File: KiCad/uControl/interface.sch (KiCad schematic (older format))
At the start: 66 parts, among them M1 MANIFOLD, P10 C3SB, P11 VSel_Vlv, P12 Valve_Conn, P13 Valve_Conn_BO, P14 Valve, P15 Flow_Conn, P16 FlowMeter, P17 Pump_Conn, P18 Pump_Conn_BO, P19 Pump_Conn_Flex, P20 Temp_Conn, P21 Temp_Conn_BO, P22 Temp, P23 Pump, P6 Pulse, P7 Gage_Pr, P8 Abso_Pr, P9 C3SB, Q1 2SD1834T100, U1 TXB0104D, U2 TXS0102DCT

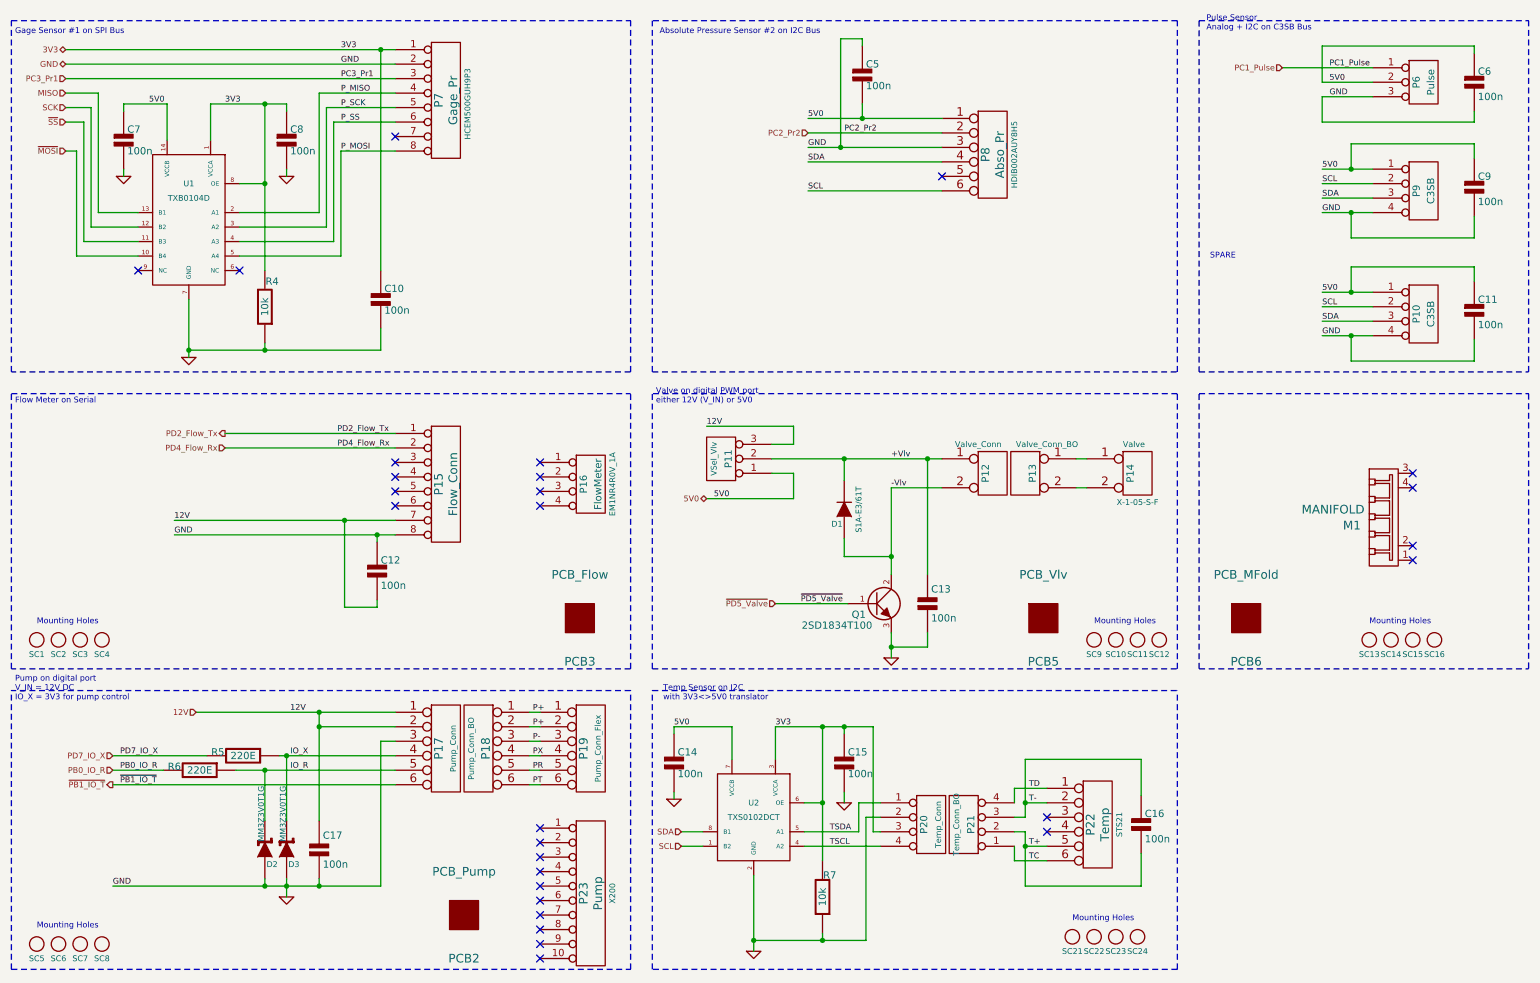
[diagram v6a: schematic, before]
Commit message: uControl track layout complete. Needs to be checked.
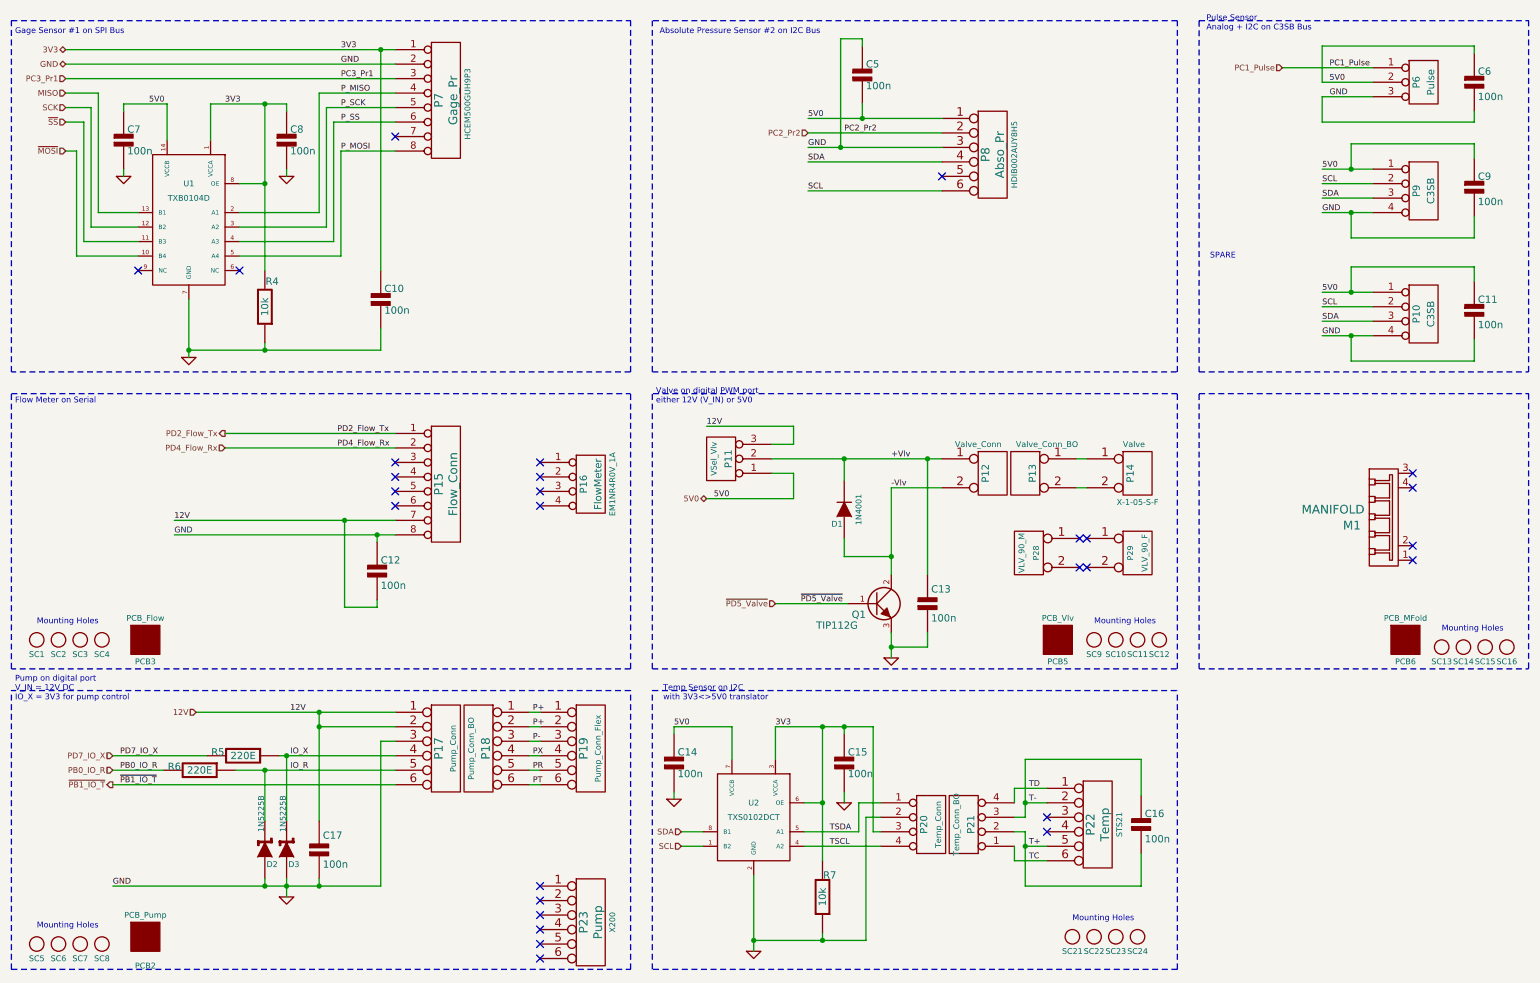
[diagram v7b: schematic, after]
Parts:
- removed P23: Pump, Pump, symbol CONN_10
- added P23: Pump, symbol CONN_6
- added P28: VLV_90_M, 2X06/90, symbol CONN_2
- added P29: VLV_90_F, Header_F_6x2, symbol CONN_2
- D1: value S1A-E3/61T -> 1N4001
- D2, D3: value MM3Z3V0T1G -> 1N5225B
- Q1: value 2SD1834T100 -> TIP112G
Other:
- moved on the sheet: PCB2, PCB3, PCB5, PCB6, SC13, SC14, SC15, SC16
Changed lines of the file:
@@
-EESchema Schematic File Version 2  date Friday 28 December 2012 10:02:48 PM IST
+EESchema Schematic File Version 2  date 12/29/2012 7:23:44 PM
 LIBS:uControl
 LIBS:Conn-raspberry
@@
 Sheet 2 5
 Title ""
-Date "28 dec 2012"
+Date "29 dec 2012"
 Rev ""
 Comp ""
@@
 Comment4 ""
 $EndDescr
+$Comp
+L CONN_6 P23
+U 1 1 50DED8EA
+P 4675 6800
+F 0 "P23" V 4625 6800 60  0000 C CNN
+F 1 "Pump" V 4725 6800 60  0000 C CNN
+F 4 "X200" V 4825 6800 40  0000 C CNN "Part_No"
+	1    4675 6800
+	1    0    0    -1
+$EndComp
+NoConn ~ 8050 4350
+NoConn ~ 8100 4350
+NoConn ~ 8100 4150
+NoConn ~ 8050 4150
+$Comp
+L CONN_2 P28
+U 1 1 50DE8768
+P 7700 4250
+F 0 "P28" V 7650 4250 40  0000 C CNN
+F 1 "VLV_90_M" V 7750 4250 40  0000 C CNN
+F 2 "2X06/90" V 7850 4250 40  0001 C CNN
+	1    7700 4250
+	-1   0    0    -1
+$EndComp
+$Comp
+L CONN_2 P29
+U 1 1 50DE8761
+P 8450 4250
+F 0 "P29" V 8400 4250 40  0000 C CNN
+F 1 "VLV_90_F" V 8500 4250 40  0000 C CNN
+F 2 "Header_F_6x2" V 8600 4250 40  0001 C CNN
+	1    8450 4250
+	1    0    0    -1
+$EndComp
 Text Label 6750 3600 0    40   ~ 0
 +Vlv
@@
 L PCB PCB6
 U 1 1 50DAE3BE
-P 9200 4700
-F 0 "PCB6" H 9200 4400 60  0000 C CNN
-F 1 "PCB_MFold" H 9200 5000 60  0000 C CNN
-F 2 "PCB_Mfold" H 9200 5100 60  0001 C CNN
-	1    9200 4700
+P 10300 4850
+F 0 "PCB6" H 10300 4700 40  0000 C CNN
+F 1 "PCB_MFold" H 10300 5000 40  0000 C CNN
+F 2 "PCB_Mfold" H 10300 5250 40  0001 C CNN
+	1    10300 4850
 	1    0    0    -1
 $EndComp
@@
 L PCB PCB5
 U 1 1 50DAE3A7
-P 7800 4700
-F 0 "PCB5" H 7800 4400 60  0000 C CNN
-F 1 "PCB_Vlv" H 7800 5000 60  0000 C CNN
-F 2 "PCB_Vlv" H 7800 5100 60  0001 C CNN
-	1    7800 4700
+P 7900 4850
+F 0 "PCB5" H 7900 4700 40  0000 C CNN
+F 1 "PCB_Vlv" H 7900 5000 40  0000 C CNN
+F 2 "PCB_Vlv" H 7900 5250 40  0001 C CNN
+	1    7900 4850
 	1    0    0    -1
 $EndComp
@@
 L PCB PCB2
 U 1 1 50DAE394
-P 3800 6750
-F 0 "PCB2" H 3800 6450 60  0000 C CNN
-F 1 "PCB_Pump" H 3800 7050 60  0000 C CNN
-F 2 "PCB_Pump" H 3800 7150 60  0001 C CNN
-	1    3800 6750
+P 1600 6900
+F 0 "PCB2" H 1600 6700 40  0000 C CNN
+F 1 "PCB_Pump" H 1600 7050 40  0000 C CNN
+F 2 "PCB_Pump" H 1600 7300 40  0001 C CNN
+	1    1600 6900
 	1    0    0    -1
 $EndComp
@@
 L PCB PCB3
 U 1 1 50DAE38C
-P 4600 4700
-F 0 "PCB3" H 4600 4400 60  0000 C CNN
-F 1 "PCB_Flow" H 4600 5000 60  0000 C CNN
-F 2 "PCB_Flow" H 4600 5100 60  0001 C CNN
-	1    4600 4700
+P 1600 4850
+F 0 "PCB3" H 1600 4700 40  0000 C CNN
+F 1 "PCB_Flow" H 1600 5000 40  0000 C CNN
+F 2 "PCB_Flow" H 1600 5250 40  0001 C CNN
+	1    1600 4850
 	1    0    0    -1
 $EndComp
@@
 Wire Notes Line
 	11150 3150 11150 5050
-Text Notes 10050 4750 0    40   ~ 0
+Text Notes 10550 4800 0    40   ~ 0
 Mounting Holes
 $Comp
 L SCREW SC16
 U 1 1 50DAD9E8
-P 10500 4850
-F 0 "SC16" H 10500 4750 40  0000 C CNN
-F 1 "SCREW" H 10500 4950 40  0001 C CNN
-F 2 "vite_3mm" H 10500 5050 40  0001 C CNN
-	1    10500 4850
+P 11000 4900
+F 0 "SC16" H 11000 4800 40  0000 C CNN
+F 1 "SCREW" H 11000 5000 40  0001 C CNN
+F 2 "vite_3mm" H 11000 5100 40  0001 C CNN
+	1    11000 4900
 	1    0    0    -1
 $EndComp
@@
 L SCREW SC15
 U 1 1 50DAD9E7
-P 10350 4850
-F 0 "SC15" H 10350 4750 40  0000 C CNN
-F 1 "SCREW" H 10350 4950 40  0001 C CNN
-F 2 "vite_3mm" H 10350 5050 40  0001 C CNN
-	1    10350 4850
+P 10850 4900
+F 0 "SC15" H 10850 4800 40  0000 C CNN
+F 1 "SCREW" H 10850 5000 40  0001 C CNN
+F 2 "vite_3mm" H 10850 5100 40  0001 C CNN
+	1    10850 4900
 	1    0    0    -1
 $EndComp
@@
 L SCREW SC14
 U 1 1 50DAD9E6
-P 10200 4850
-F 0 "SC14" H 10200 4750 40  0000 C CNN
-F 1 "SCREW" H 10200 4950 40  0001 C CNN
-F 2 "vite_3mm" H 10200 5050 40  0001 C CNN
-	1    10200 4850
+P 10700 4900
+F 0 "SC14" H 10700 4800 40  0000 C CNN
+F 1 "SCREW" H 10700 5000 40  0001 C CNN
+F 2 "vite_3mm" H 10700 5100 40  0001 C CNN
+	1    10700 4900
 	1    0    0    -1
 $EndComp
@@
 L SCREW SC13
 U 1 1 50DAD9E5
-P 10050 4850
-F 0 "SC13" H 10050 4750 40  0000 C CNN
-F 1 "SCREW" H 10050 4950 40  0001 C CNN
-F 2 "vite_3mm" H 10050 5050 40  0001 C CNN
-	1    10050 4850
+P 10550 4900
+F 0 "SC13" H 10550 4800 40  0000 C CNN
+F 1 "SCREW" H 10550 5000 40  0001 C CNN
+F 2 "vite_3mm" H 10550 5100 40  0001 C CNN
+	1    10550 4900
 	1    0    0    -1
 $EndComp
@@
 NoConn ~ 4325 6750
 $Comp
-L CONN_10 P23
-U 1 1 50D6C18B
-P 4675 6600
-F 0 "P23" V 4625 6600 60  0000 C CNN
-F 1 "Pump" V 4725 6600 60  0000 C CNN
-F 2 "Pump" V 4825 6600 60  0001 C CNN
-F 4 "X200" V 4825 6600 40  0000 C CNN "Part_No"
-	1    4675 6600
-	1    0    0    -1
-$EndComp
-$Comp
 L CONN_4 P16
 U 1 1 50D6BF9C
@@
 NoConn ~ 4325 6650
 NoConn ~ 4325 6550
-NoConn ~ 4325 6450
-NoConn ~ 4325 6350
-NoConn ~ 4325 6250
-NoConn ~ 4325 6150
 NoConn ~ 4325 3925
 NoConn ~ 4325 3825
@@
 P 2425 6300
 F 0 "D2" V 2325 6250 40  0000 C CNN
-F 1 "MM3Z3V0T1G" H 2675 6325 40  0000 C CNN
+F 1 "1N5225B" H 2675 6325 40  0000 C CNN
 F 2 "diode_do35" H 2675 6350 40  0001 C CNN
 	1    2425 6300
@@
 P 6425 3950
 F 0 "D1" V 6325 4000 40  0000 C CNN
-F 1 "S1A-E3/61T" H 6425 3850 40  0000 C CNN
+F 1 "1N4001" H 6425 3850 40  0000 C CNN
 F 2 "diode_do41" H 6425 3950 40  0001 C CNN
 	1    6425 3950
@@
 P 6650 4600
 F 0 "Q1" H 6525 4525 50  0000 C CNN
-F 1 "2SD1834T100" H 6375 4450 50  0000 C CNN
+F 1 "TIP112G" H 6375 4450 50  0000 C CNN
 F 2 "TO220-3-V" H 6840 4600 30  0001 C CNN
 	1    6650 4600
@@
 P 2575 6300
 F 0 "D3" V 2475 6250 40  0000 C CNN
-F 1 "MM3Z3V0T1G" H 2825 6325 40  0000 C CNN
+F 1 "1N5225B" H 2825 6325 40  0000 C CNN
 F 2 "diode_do35" H 2825 6350 40  0001 C CNN
 	1    2575 6300

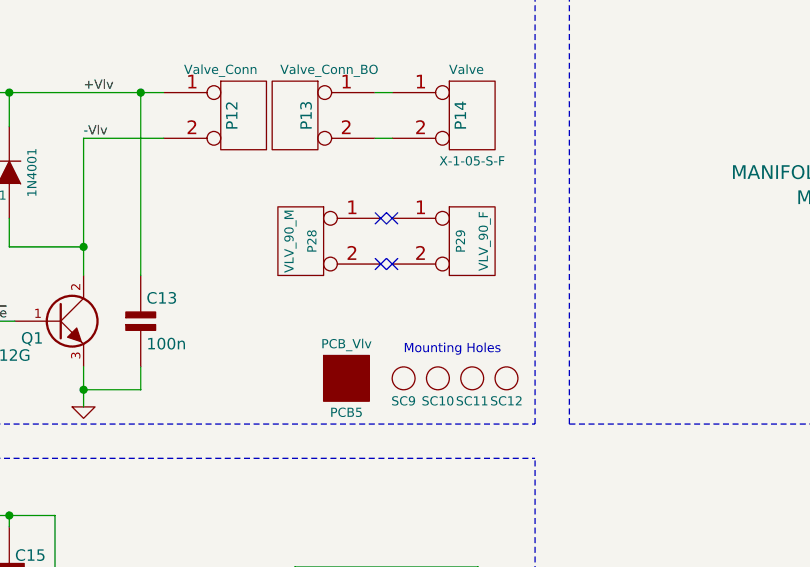
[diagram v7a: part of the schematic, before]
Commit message: uControl - track layout done. Silk legend almost done.
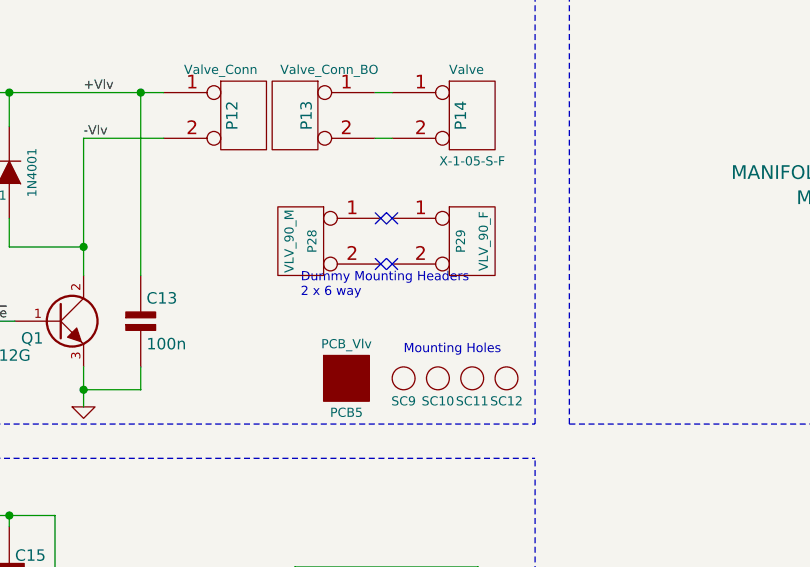
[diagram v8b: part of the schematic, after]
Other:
- note added: "Dummy Mounting Headers\n2 x 6 way"
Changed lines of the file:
@@
-EESchema Schematic File Version 2  date 12/29/2012 7:23:44 PM
+EESchema Schematic File Version 2  date Sunday 30 December 2012 01:31:03 AM IST
 LIBS:uControl
 LIBS:Conn-raspberry
@@
 Comment4 ""
 $EndDescr
+Text Notes 7700 4500 0    40   ~ 0
+Dummy Mounting Headers\n2 x 6 way
 $Comp
 L CONN_6 P23
